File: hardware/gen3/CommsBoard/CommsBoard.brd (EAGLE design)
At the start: 140 x 107 mm, 41 parts, among them U1 ATMEGA165PV-8AU

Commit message: finished pour and DRC
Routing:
- net 12V: track 0.00 -> 10.5 mm
- net 12VGND: track 0.00 -> 10.5 mm
- net SCK: track 88.0 -> 78.1 mm, vias 1 -> 2
- net MOSI: track 91.8 -> 98.1 mm
- net GND: track 186.0 -> 180.4 mm
- net 5V: track 0.00 -> 2.63 mm
- net MISO: vias 1 -> 2

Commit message: hooked up ss lines
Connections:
- removed net SS1: SPI_HEADER.4
- removed net SS2: SPI_HEADER.5
- removed net SS3: SPI_HEADER.6
- removed net SS4: SPI_HEADER.7
- removed net SS5: SPI_HEADER.8
- new net SS_E1: SPI_HEADER.6, U1.59
- new net SS_E2: SPI_HEADER.7, U1.58
- new net SS_E3: SPI_HEADER.8, U1.57
- new net SS_K: SPI_HEADER.5, U1.60
- new net SS_M: SPI_HEADER.4, U1.61
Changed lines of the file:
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@@
 <?xml version="1.0" encoding="utf-8"?>
 <!DOCTYPE eagle SYSTEM "eagle.dtd">
-<eagle version="6.4">
+<eagle version="7.2.0">
 <drawing>
 <settings>
@@
 <pass name="Default">
 <param name="RoutingGrid" value="12.5mil"/>
+<param name="AutoGrid" value="1"/>
+<param name="Efforts" value="0"/>
+<param name="TopRouterVariant" value="1"/>
 <param name="tpViaShape" value="round"/>
 <param name="PrefDir.1" value="*"/>
@@
 <via x="73.025" y="22.5425" extent="1-16" drill="0.6096"/>
 </signal>
-<signal name="SS1">
+<signal name="SS_M">
 <contactref element="SPI_HEADER" pad="4"/>
-</signal>
-<signal name="SS2">
+<contactref element="U1" pad="61"/>
+<wire x1="79.38" y1="43.3932" x2="116" y2="72.38" width="0" layer="19" extent="1-1"/>
+</signal>
+<signal name="SS_K">
 <contactref element="SPI_HEADER" pad="5"/>
-</signal>
-<signal name="SS5">
+<contactref element="U1" pad="60"/>
+<wire x1="79.38" y1="44.206" x2="116" y2="69.84" width="0" layer="19" extent="1-1"/>
+</signal>
+<signal name="SS_E3">
 <contactref element="SPI_HEADER" pad="8"/>
+<contactref element="U1" pad="57"/>
+<wire x1="79.38" y1="46.5936" x2="116" y2="62.22" width="0" layer="19" extent="1-1"/>
 </signal>
 <signal name="MOSI">
@@
 <wire x1="116" y1="80" x2="110.9" y2="80" width="0.254" layer="16"/>
 </signal>
-<signal name="SS4">
+<signal name="SS_E2">
 <contactref element="SPI_HEADER" pad="7"/>
-</signal>
-<signal name="SS3">
+<contactref element="U1" pad="58"/>
+<wire x1="79.38" y1="45.8062" x2="116" y2="64.76" width="0" layer="19" extent="1-1"/>
+</signal>
+<signal name="SS_E1">
 <contactref element="SPI_HEADER" pad="6"/>
+<contactref element="U1" pad="59"/>
+<wire x1="79.38" y1="44.9934" x2="116" y2="67.3" width="0" layer="19" extent="1-1"/>
 </signal>
 <signal name="XBRST">

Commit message: fixed current limiting
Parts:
- C1, C2: value 100nF -> .1uF
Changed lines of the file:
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@@
 <attribute name="PROD_ID" value="CONN-11563" x="116" y="27" size="1.778" layer="27" rot="R270" display="off"/>
 </element>
-<element name="C1" library="SparkFun-Capacitors" package="0805" value="100nF" x="75" y="43"/>
-<element name="C2" library="SparkFun-Capacitors" package="0805" value="100nF" x="75" y="39"/>
+<element name="C1" library="SparkFun-Capacitors" package="0805" value=".1uF" x="75" y="43"/>
+<element name="C2" library="SparkFun-Capacitors" package="0805" value=".1uF" x="75" y="39"/>
 <element name="R1" library="SparkFun-Passives" package="0805" value="10k" x="78" y="37" rot="R270"/>
 <element name="R2" library="SparkFun-Passives" package="0805" value="10k" x="110" y="80" rot="MR180"/>

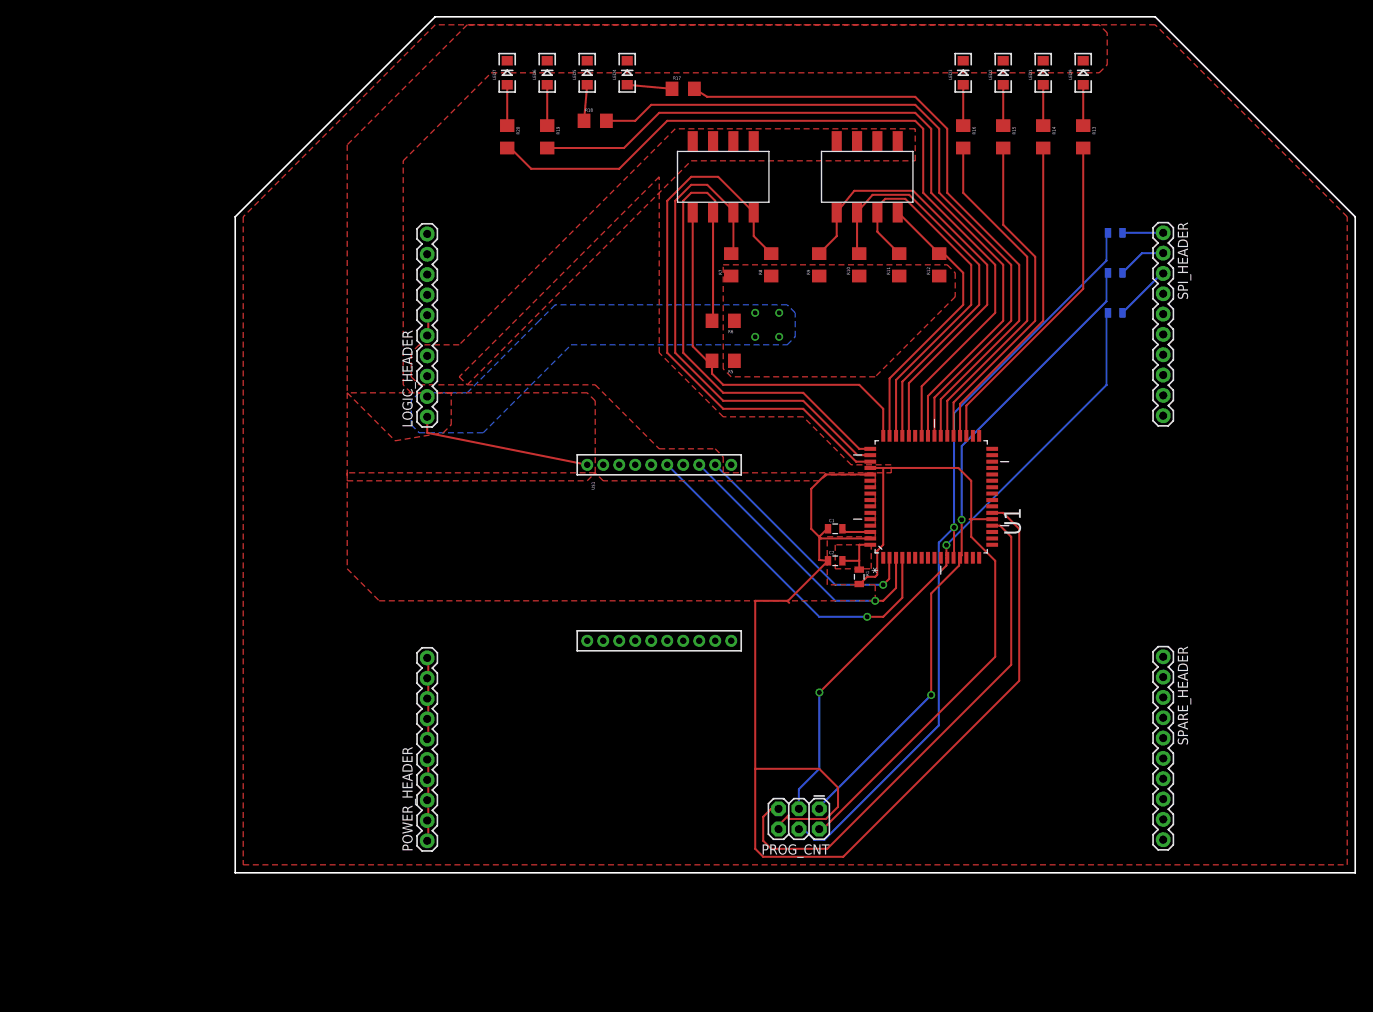
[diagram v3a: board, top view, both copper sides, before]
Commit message: most packages replaced
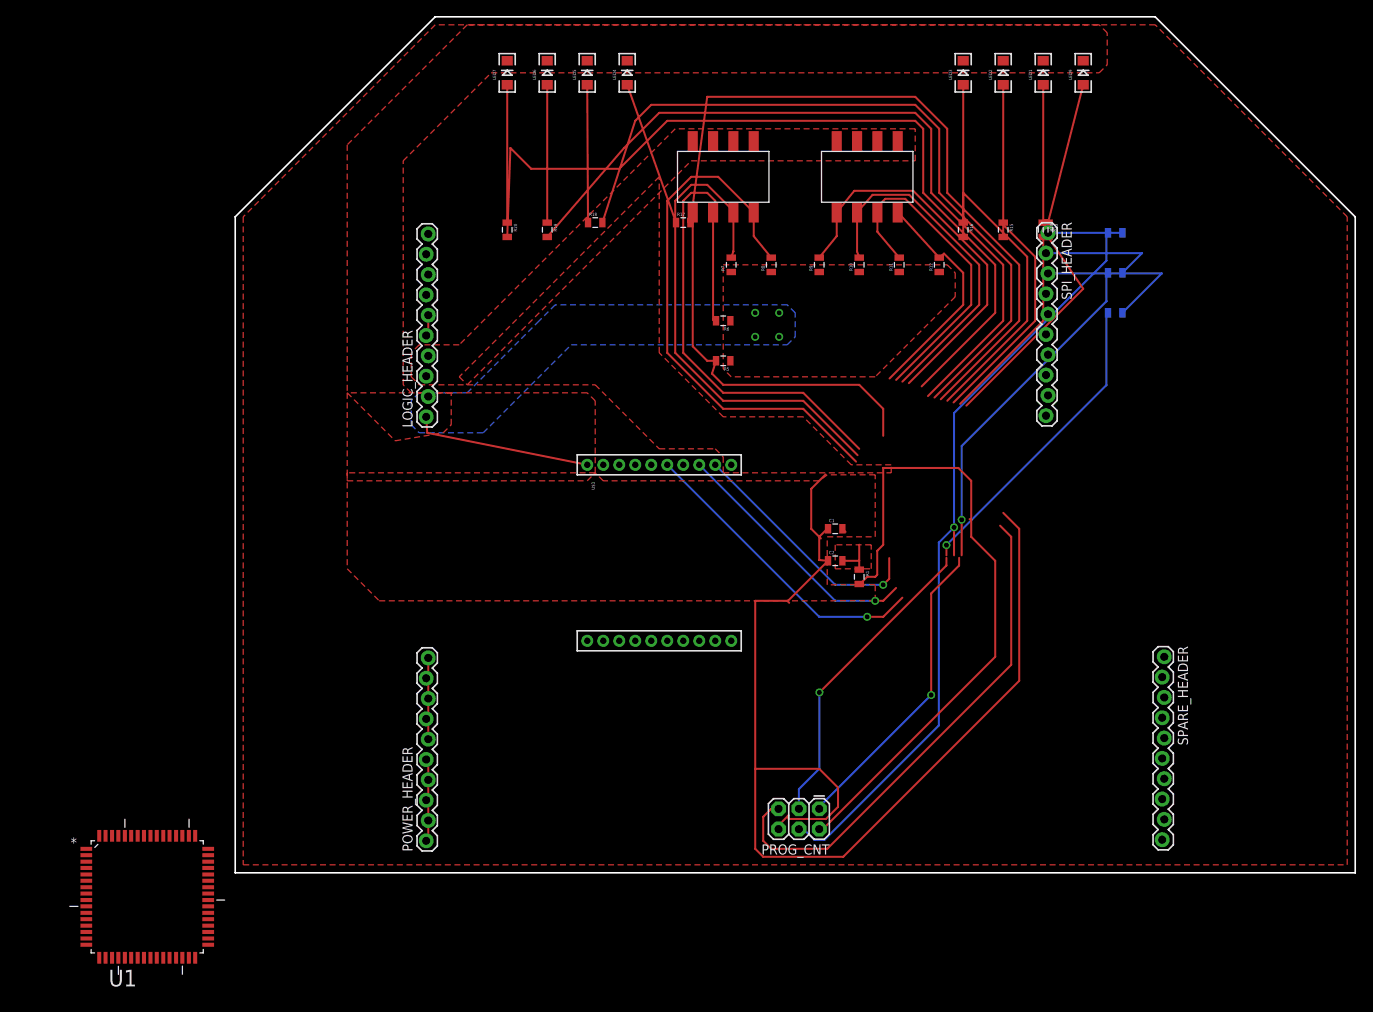
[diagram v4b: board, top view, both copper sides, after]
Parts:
- LOGIC_HEADER, POWER_HEADER, SPARE_HEADER, SPI_HEADER: value M10SILK_FEMALE_PTH -> M10LOCK; device SparkFun-Connectors:1X10 -> SparkFun-Connectors:1X10_LOCK
- R10, R11, R12, R13, R14, R15, R16, R17, R18, R19, R20, R5, R6, R7, R8, R9: device SparkFun-Passives:1206 -> SparkFun-Passives:0805
- U1: device Atmel_By_element14_Batch_1-00:QFP80P1600X1600X120-64N -> gen3:QFP80P1600X1600X120-64N
- moved U1 110.0 mm to (-11.0, -3.00), turned to 0 degrees
- moved R17 16.7 mm to (56.0, 81.3)
- moved SPI_HEADER 14.5 mm to (101.5, 80.0)
- moved R18 12.7 mm to (45.0, 81.3)
- moved R13 12.4 mm to (101.6, 80.4)
- moved R14 11.6 mm to (101.0, 80.4)
- moved R15 11.6 mm to (96.0, 80.4)
- moved R16 11.6 mm to (91.0, 80.4)
- moved R19 11.6 mm to (39.0, 80.4)
- moved R20 11.6 mm to (34.0, 80.4)
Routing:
- net RLED1: track 40.3 -> 25.2 mm
- net N$4: track 7.14 -> 21.2 mm
- net GLED1: track 42.0 -> 28.5 mm
- net GND: track 180.4 -> 167.3 mm
- net N$9: track 4.52 -> 17.2 mm
- net N$1: track 5.10 -> 17.8 mm
- net N$8: track 5.62 -> 18.3 mm
- net GLED2: track 41.9 -> 29.6 mm
- net N$7: track 5.10 -> 17.2 mm
- net N$6: track 5.10 -> 17.2 mm
- net N$5: track 5.10 -> 17.2 mm
- net N$11: track 5.10 -> 17.2 mm
- net N$10: track 5.10 -> 17.2 mm
- net GLED3: track 79.7 -> 89.1 mm
- net N$3: track 6.12 -> 15.5 mm
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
